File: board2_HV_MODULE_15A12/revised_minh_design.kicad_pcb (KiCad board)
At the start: 2 copper layers, 100.1 x 56.6 mm, 24 parts, among them J1 Conn_01x07_Male, J2 Conn_01x01_Male, U1 LM7805_TO220, U2 NE5532, U4 15A12

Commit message: JLCPCB Submission for 15A12 board
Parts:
- U4: footprint Converter_DCDC:Advanced Energy 15A12P4 -> Library:Advanced Energy 15A12P4
- moved D2 2.45 mm to (180.2, 35.0), turned to 90 degrees
- moved R6 1.14 mm to (174.8, 26.5)
- moved R5 1.14 mm to (171.4, 36.7)
- moved C2 0.30 mm to (175.4, 64.8)
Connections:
- J1 pad 3: DAC_SIG -> ENABLE
- J1 pad 6: VPGM -> DAC_SIG
- J1 pad 7: SGND -> VPGM
- U4 pad 4: unconnected-(U4-Pad4) -> ENABLE
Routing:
- net ENABLE: track 0.00 -> 52.0 mm
- net DAC_SIG: track 30.4 -> 23.3 mm
- net Net-(D2-Pad1): track 6.19 -> 9.47 mm
- net VPGM: track 45.7 -> 44.4 mm
- net VMON_3V3: track 34.8 -> 35.8 mm
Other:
- board size 100.1 x 56.6 mm -> 99.6 x 56.6 mm

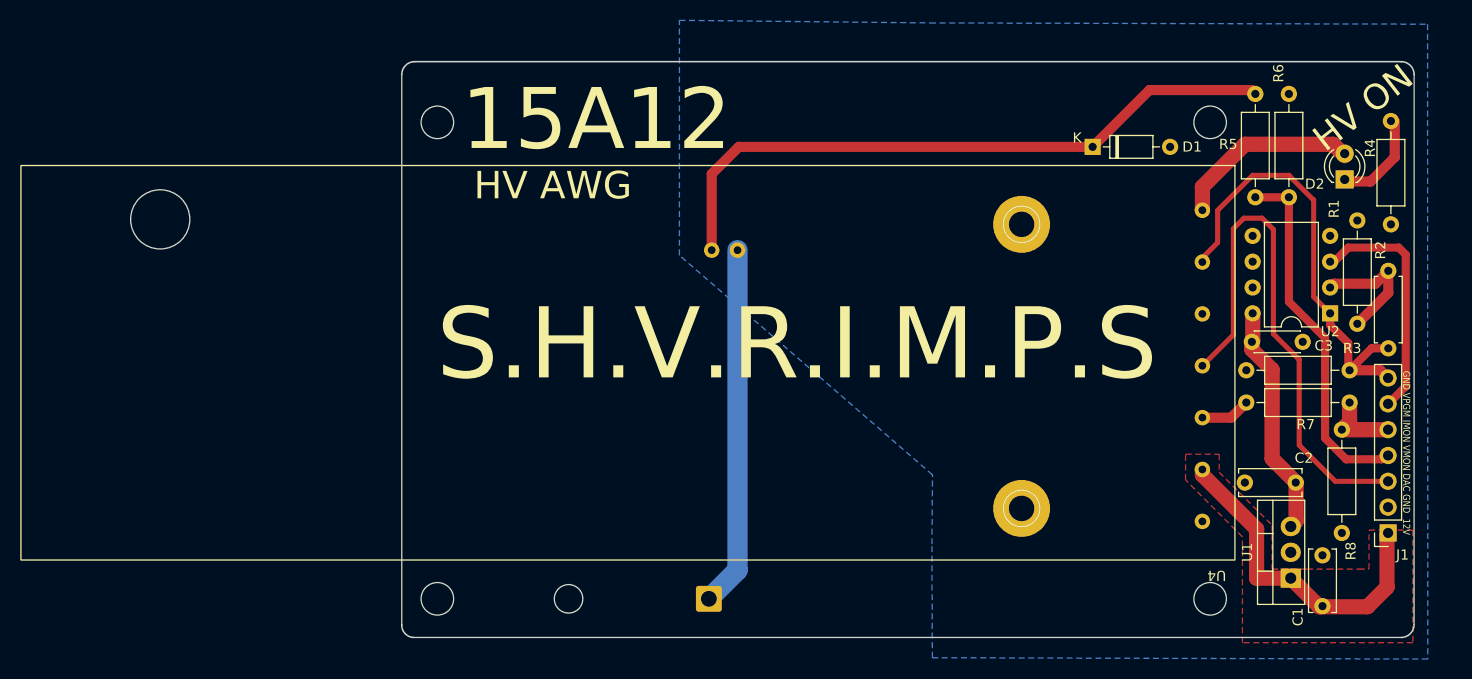
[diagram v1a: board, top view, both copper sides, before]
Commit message: JLCPCB Submission for 15A12 board, double row connectors added, separate power and signal connectors
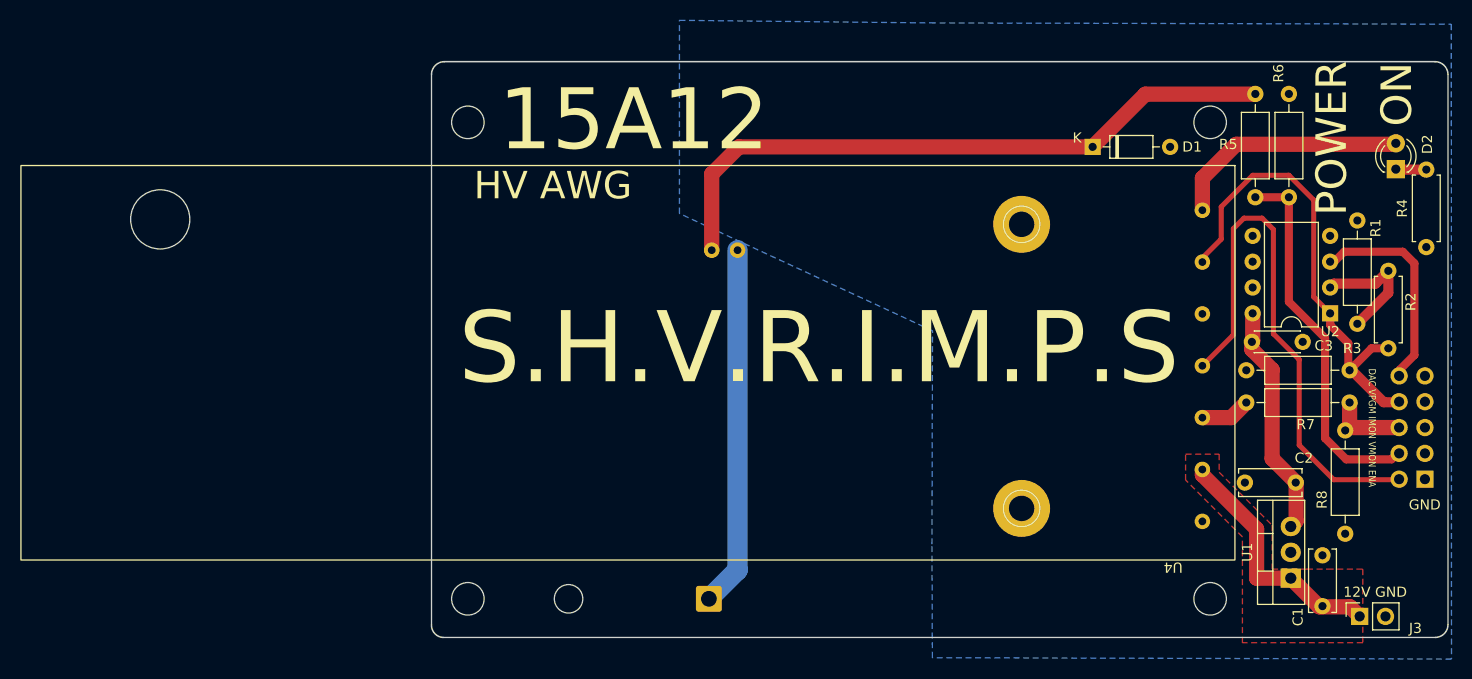
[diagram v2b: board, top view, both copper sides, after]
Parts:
- added J3: Conn_01x02_Male, Connector_PinSocket_2.54mm:PinSocket_1x02_P2.54mm_Vertical, F.Cu at (181.7, 77.9)
- J1: footprint Connector_PinSocket_2.54mm:PinSocket_1x07_P2.54mm_Vertical -> Connector_PinSocket_2.54mm:PinSocket_2x05_P2.54mm_Vertical; moved to B.Cu
- R4: footprint Resistor_THT:R_Axial_DIN0207_L6.3mm_D2.5mm_P10.16mm_Horizontal -> Resistor_THT:R_Axial_DIN0207_L6.3mm_D2.5mm_P7.62mm_Horizontal
- moved J1 6.41 mm to (188.1, 64.4), turned to 0 degrees
- moved D2 5.13 mm to (185.3, 33.9)
- moved R4 4.14 mm to (188.3, 41.6)
- moved   3.00 mm to (94.0, 76.2)
- moved   3.00 mm to (94.0, 29.3)
- moved R8 0.34 mm to (180.3, 69.8)
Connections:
- J1 pad 1: +12V -> SGND
- J1 pad 2: SGND -> ENABLE
- J1 pad 3: ENABLE -> SGND
- J1 pad 5: IMON_3V3 -> SGND
- J1 pad 6: DAC_SIG -> IMON_3V3
- J1 pad 7: VPGM -> SGND
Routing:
- net +12V: track 33.1 -> 24.6 mm
- net Net-(D2-Pad1): track 9.47 -> 3.02 mm
- net Net-(D2-Pad2): track 18.5 -> 23.6 mm
- net DAC_SIG: track 23.3 -> 20.5 mm
- net VPGM: track 44.4 -> 46.1 mm
- net VMON_3V3: track 35.8 -> 36.8 mm
- net ENABLE: track 52.0 -> 53.0 mm
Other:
- board size 99.6 x 56.6 mm -> 100 x 56.6 mm
- board text added: "12V GND"
- board text added: "DAC VPGM IMON VMON ENA"
- board text added: "GND"
- board text added: "ON"
- board text added: "POWER"
- board text removed: "GND VPGM IMON VMON DAC GND 12V"
- board text removed: "HV ON"
